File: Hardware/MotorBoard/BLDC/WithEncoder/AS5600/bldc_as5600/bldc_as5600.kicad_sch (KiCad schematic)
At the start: 1 part, among them U1 AS5600-ASOT

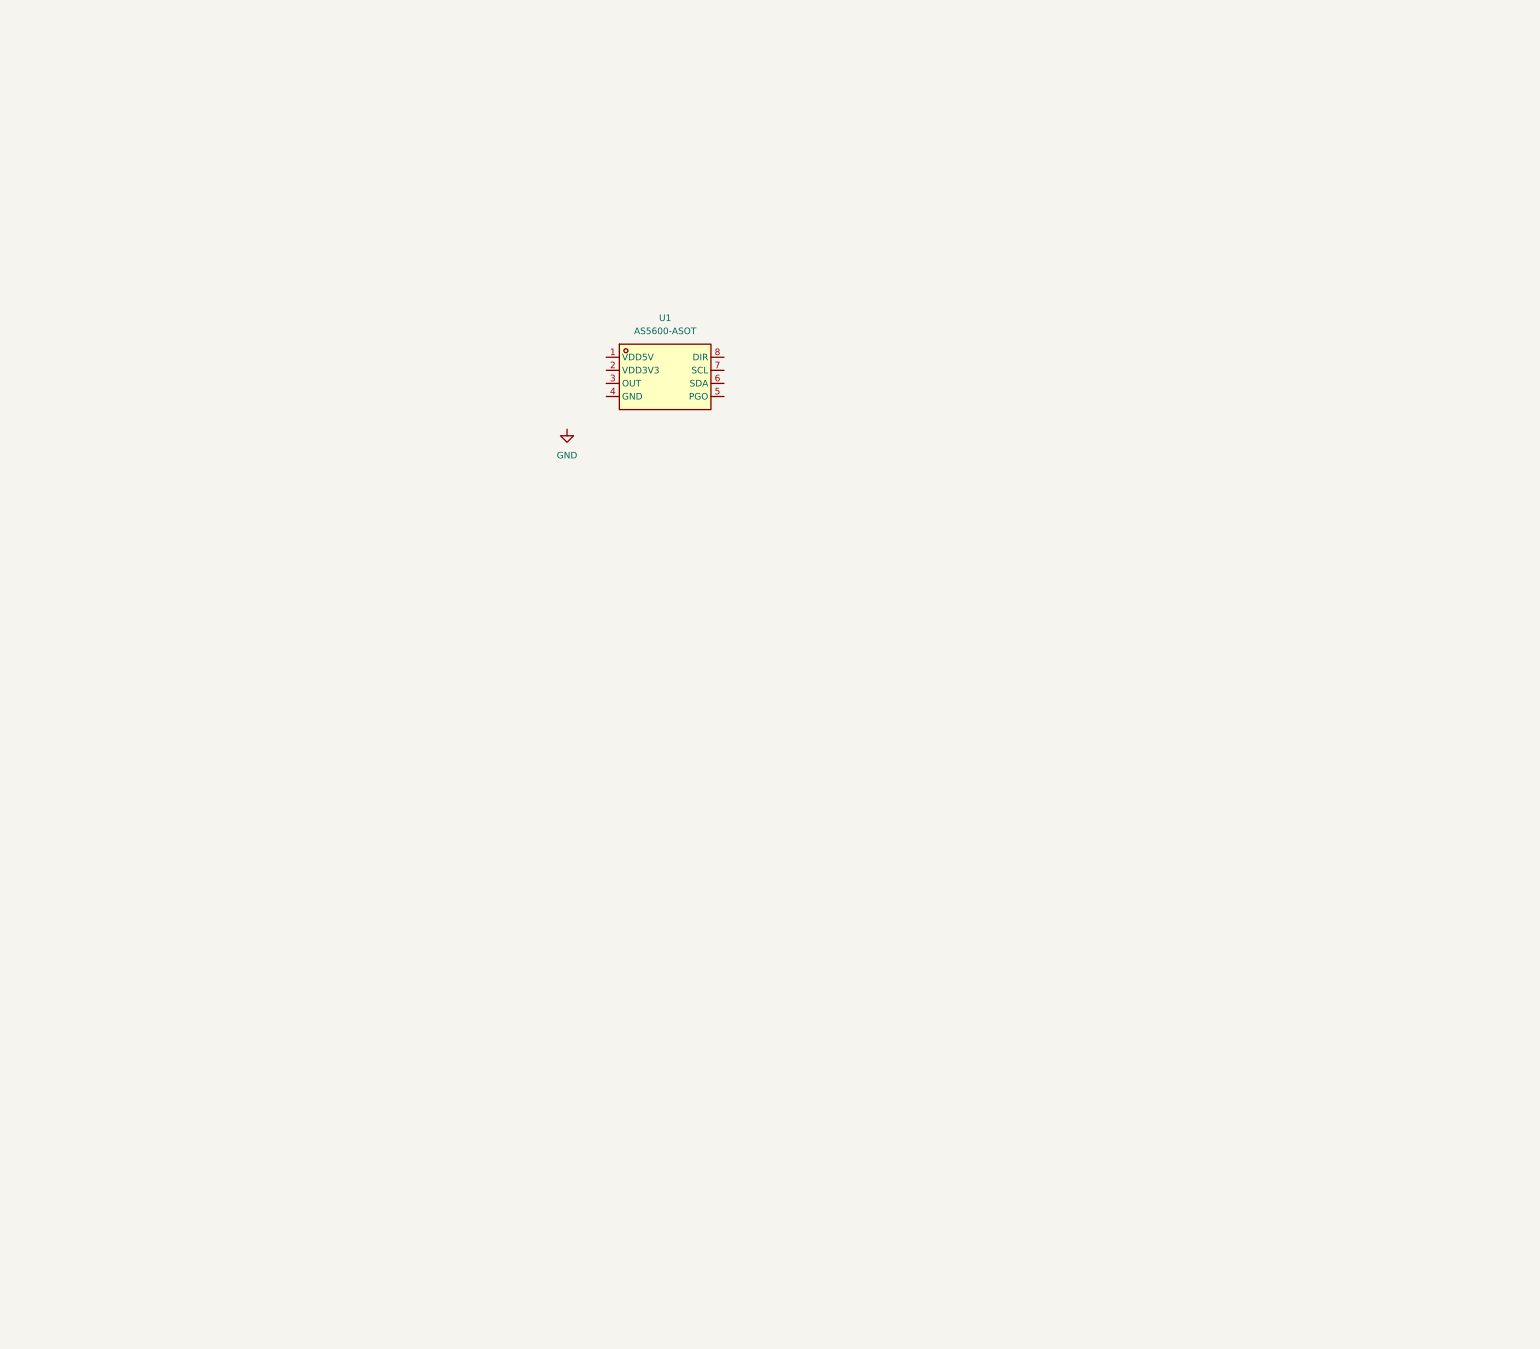
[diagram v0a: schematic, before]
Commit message: started layout of encoder module
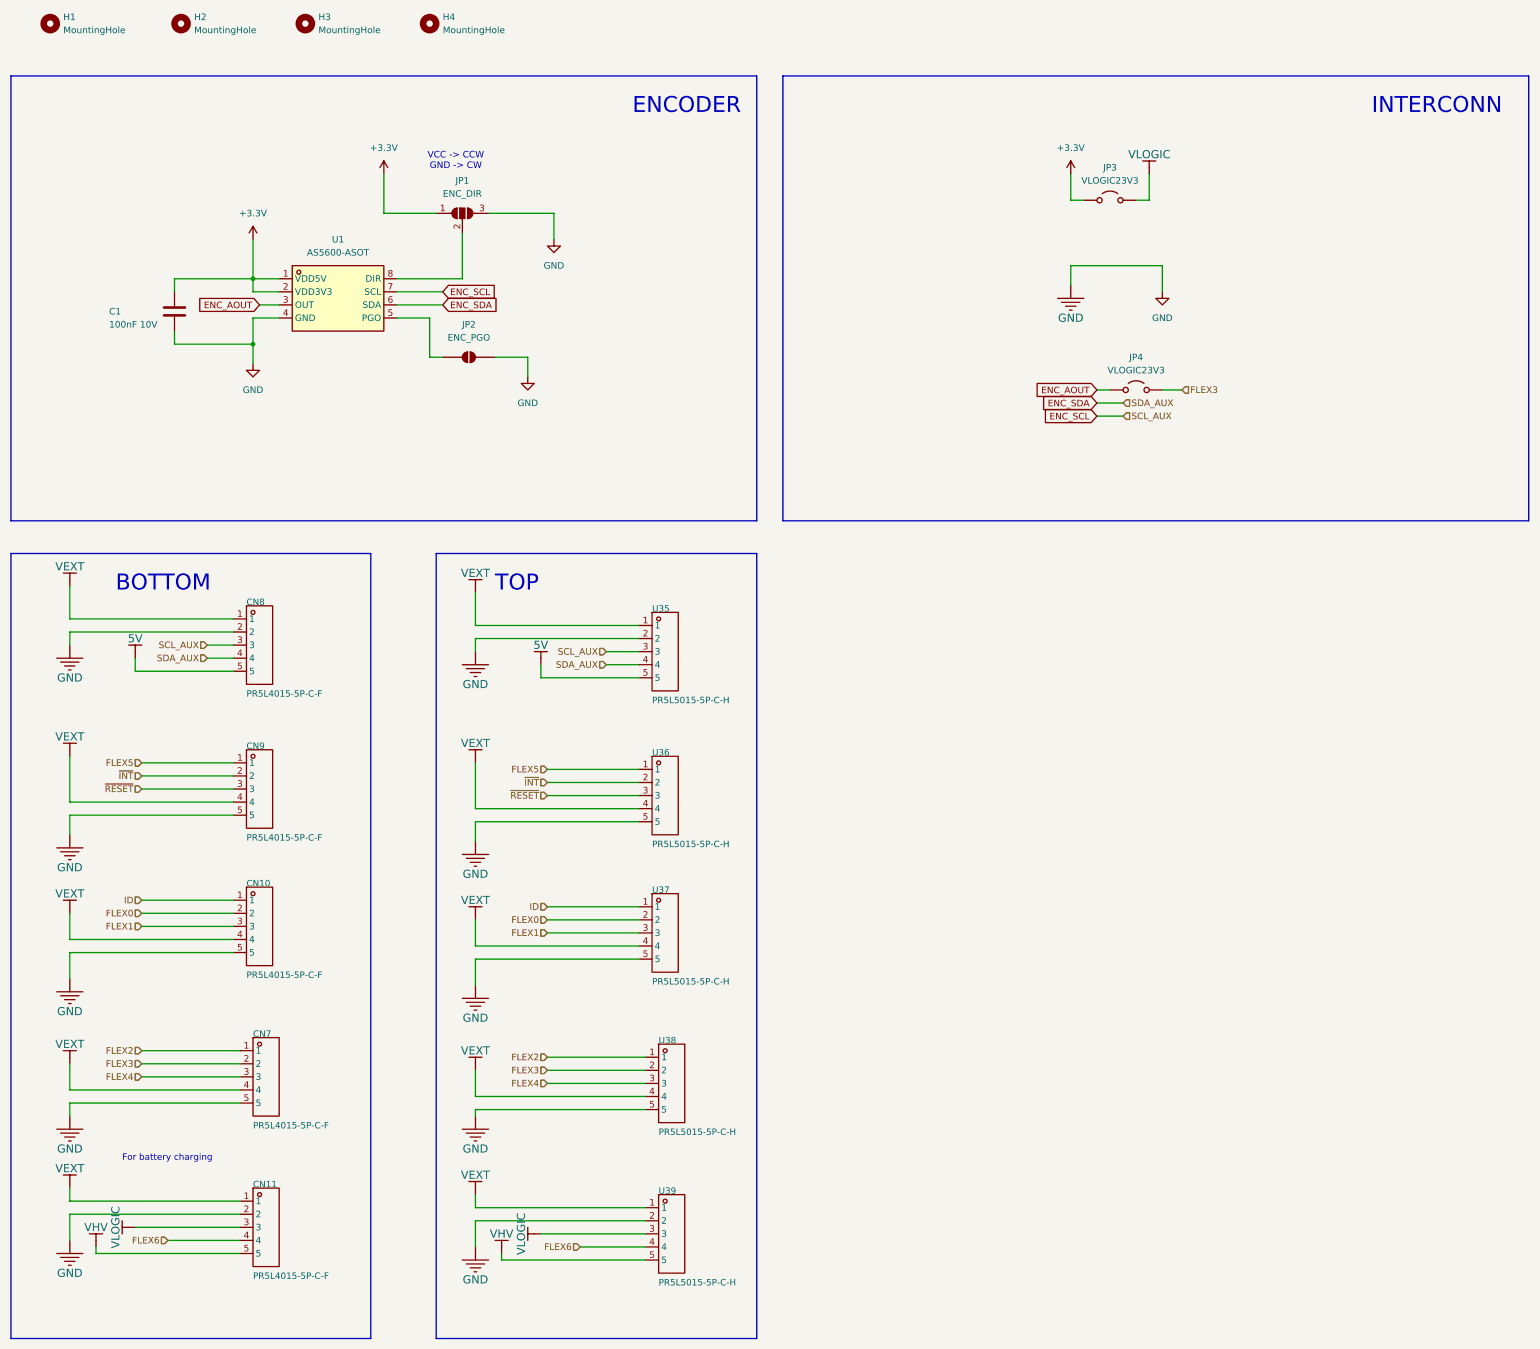
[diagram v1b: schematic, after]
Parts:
- added C1: 100nF 10V, SpaghettiLAB:C0603, symbol Device:C
- added CN10, CN11, CN7, CN8, CN9: PR5L4015-5P-C-F, SpaghettiLAB:CONN-TH_PR5L4015-5P-C-F, symbol USBC_PD_mo-easyedapro:PR5L4015-5P-C-F
- added H1, H2, H3, H4: MountingHole, MountingHole:MountingHole_2.2mm_M2, symbol Mechanical:MountingHole
- added JP1: ENC_DIR, Jumper:SolderJumper-3_P1.3mm_Open_Pad1.0x1.5mm, symbol Jumper:SolderJumper_3_Open
- added JP2: ENC_PGO, Jumper:SolderJumper-2_P1.3mm_Open_Pad1.0x1.5mm, symbol Jumper:SolderJumper_2_Open
- added JP3: VLOGIC23V3, Jumper:SolderJumper-2_P1.3mm_Open_Pad1.0x1.5mm, symbol Jumper:Jumper_2_Open
- added JP4: VLOGIC23V3, Connector_PinSocket_2.54mm:PinSocket_1x02_P2.54mm_Vertical, symbol Jumper:Jumper_2_Open
- added U35, U36, U37, U38, U39: PR5L5015-5P-C-H, SpaghettiLAB:CONN-TH_PR5L5015-5P-C-H, symbol USBC_PD_mo-easyedapro:PR5L5015-5P-C-H
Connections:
- net GND: now also U1.4 (GND), C1.2, CN10.5, CN11.2, CN7.5, CN8.2, CN9.5, JP1.3 (B), JP2.2 (B), U35.2, U36.5, U37.5, U38.5, U39.2
- net +3.3V: now reaches U1.1 (VDD5V)
- net +3.3V: now also U1.2 (VDD3V3), C1.1, JP1.1 (A), JP3.1 (A)
- net ENC_AOUT: now reaches U1.3 (OUT)
- net ENC_AOUT: now also JP4.1 (A)
- net at U1.5 (PGO): now also JP2.1 (A)
- net ENC_SDA: now reaches U1.6 (SDA)
- net ENC_SDA: now also CN8.4, U35.4
- net ENC_SCL: now reaches U1.7 (SCL)
- net ENC_SCL: now also CN8.3, U35.3
- net at U1.8 (DIR): now also JP1.2 (C)
- new net 5V: CN8.5, U35.5
- new net FLEX0: CN10.2, U37.2
- new net FLEX1: CN10.3, U37.3
- new net FLEX2: CN7.1, U38.1
- new net FLEX3: CN7.2, JP4.2 (B), U38.2
- new net FLEX4: CN7.3, U38.3
- new net FLEX5: CN9.1, U36.1
- new net FLEX6: CN11.4, U39.4
- new net ID: CN10.1, U37.1
- new net VEXT: CN10.4, CN11.1, CN7.4, CN8.1, CN9.4, U35.1, U36.4, U37.4, U38.4, U39.1
- new net VHV: CN11.5, U39.5
- new net VLOGIC: CN11.3, JP3.2 (B), U39.3
- new net ~{INT}: CN9.2, U36.2
- new net ~{RESET}: CN9.3, U36.3
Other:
- note added: "BOTTOM"
- note added: "ENCODER"
- note added: "For battery charging"
- note added: "INTERCONN"
- note added: "TOP"
- note added: "VCC -> CCW GND -> CW"
- moved on the sheet: U1

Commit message: Done layout for as5600 encoder board
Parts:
- removed JP1: ENC_DIR, Jumper:SolderJumper-3_P1.3mm_Open_Pad1.0x1.5mm, symbol Jumper:SolderJumper_3_Open
- removed JP3: VLOGIC23V3, Jumper:SolderJumper-2_P1.3mm_Open_Pad1.0x1.5mm, symbol Jumper:Jumper_2_Open
- removed JP4: VLOGIC23V3, Connector_PinSocket_2.54mm:PinSocket_1x02_P2.54mm_Vertical, symbol Jumper:Jumper_2_Open
- added JP4: ENC_PGO, Jumper:SolderJumper-2_P1.3mm_Open_Pad1.0x1.5mm, symbol Jumper:SolderJumper_2_Open
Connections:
- net VLOGIC is gone; now on net +3.3V: CN11.3, U39.3
- net ENC_AOUT: now also JP4.1 (A)
- net FLEX3: now also JP4.2 (B)
- net GND: now also U1.8 (DIR)

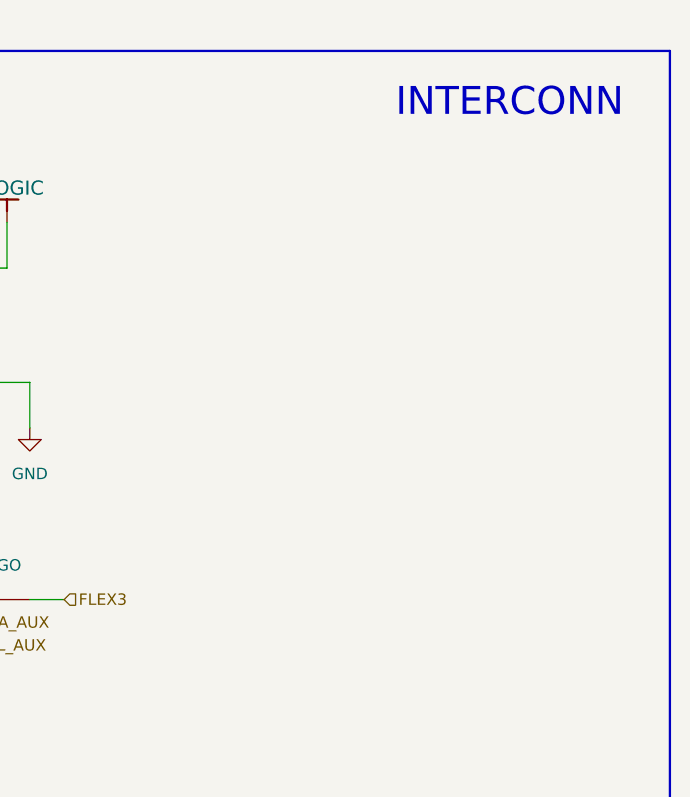
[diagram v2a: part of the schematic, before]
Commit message: Added JST for UART to display module
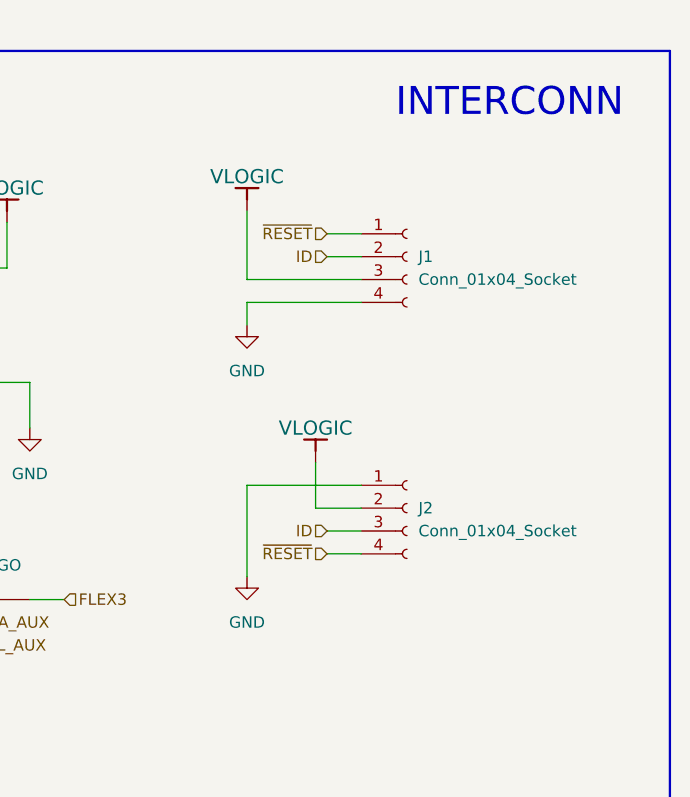
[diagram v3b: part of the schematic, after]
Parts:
- added J1, J2: Conn_01x04_Socket, symbol Connector:Conn_01x04_Socket
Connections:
- net +3.3V: now also J1.3 (Pin_3), J2.2 (Pin_2)
- net GND: now also J1.4 (Pin_4), J2.1 (Pin_1)
- net ID: now also J1.2 (Pin_2), J2.3 (Pin_3)
- net ~{RESET}: now also J1.1 (Pin_1), J2.4 (Pin_4)

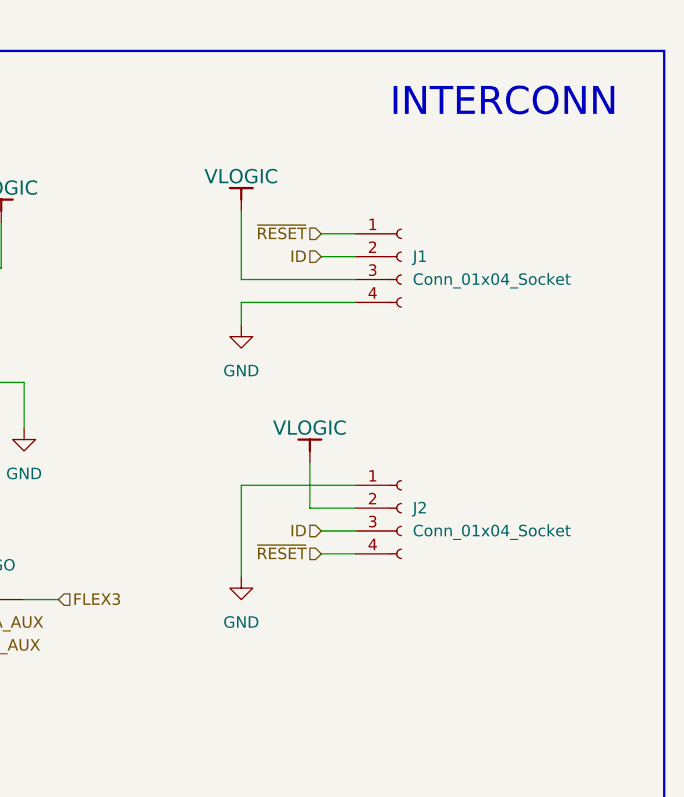
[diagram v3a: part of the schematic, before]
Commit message: removed a jst in encoder board
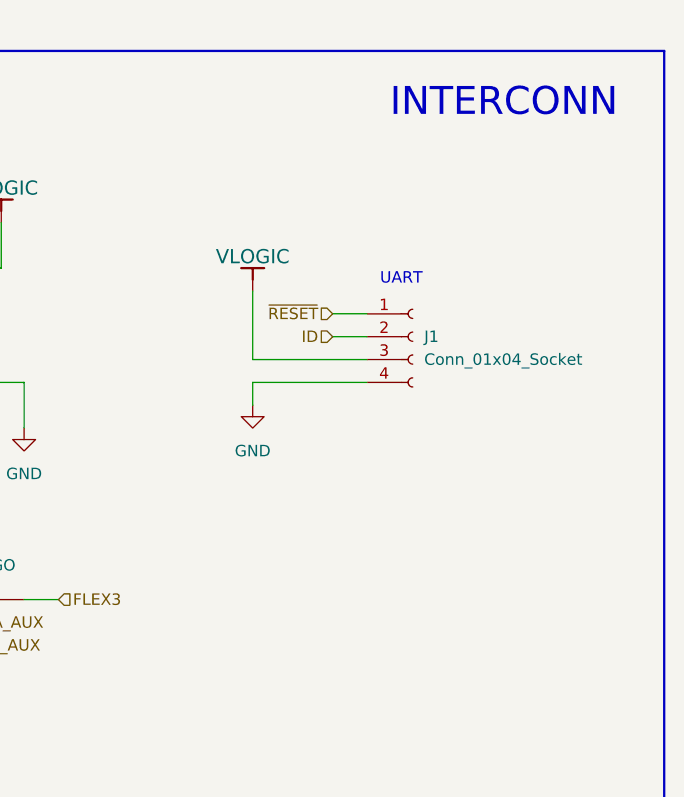
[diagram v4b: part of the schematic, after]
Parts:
- removed J2: Conn_01x04_Socket, symbol Connector:Conn_01x04_Socket
- J1: footprint (none) -> Connector_JST:JST_GH_SM04B-GHS-TB_1x04-1MP_P1.25mm_Horizontal
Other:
- note added: "UART"
- moved on the sheet: J1
